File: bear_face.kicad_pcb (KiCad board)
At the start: 2 copper layers, 301.7 x 112.6 mm, 275 parts, among them J1 USB_B_Micro, Q1 2N7002, SW1 SW_Push, U1 ATmega32U4-AU, Y1 16MHz

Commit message: Short diode, resistor tracks added for ease of starting over
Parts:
- moved R8 0.79 mm to (219.8, 88.2)
- turned R64 to 180 degrees
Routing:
- net Net-(MX81-Pad4): track 0.00 -> 23.1 mm
- net Net-(MX78-Pad4): track 0.00 -> 21.8 mm
- net Net-(MX65-Pad4): track 0.00 -> 21.8 mm
- net Net-(MX64-Pad4): track 0.00 -> 21.8 mm
- net Net-(MX63-Pad4): track 0.00 -> 21.8 mm
- net Net-(MX75-Pad4): track 0.00 -> 21.8 mm
- net Net-(MX79-Pad4): track 0.00 -> 21.8 mm
- net Net-(MX80-Pad4): track 0.00 -> 21.8 mm
- net Net-(MX77-Pad4): track 0.00 -> 21.8 mm
- net Net-(MX76-Pad4): track 0.00 -> 21.8 mm
- net Net-(MX82-Pad4): track 0.00 -> 19.8 mm
- net Net-(MX83-Pad4): track 0.00 -> 14.9 mm
- net Net-(MX74-Pad4): track 0.00 -> 14.9 mm
- net Net-(D72-Pad2): track 0.00 -> 13.2 mm
- net Net-(D73-Pad2): track 0.00 -> 13.2 mm
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
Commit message: Short traces flipped
Flipped short trace from LED to resistor to B.Cu
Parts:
- moved Q1 10.3 mm to (96.0, 160.4)
- moved R88 5.55 mm to (96.0, 151.7), turned to 90 degrees
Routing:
- net ROW0: track 0.00 -> 303.8 mm
- net +5V: track 0.00 -> 303.2 mm
- net LEDOUT: track 0.00 -> 294.2 mm
- net Net-(MX81-Pad4): track 23.1 -> 0.00 mm
- net Net-(MX78-Pad4): track 21.8 -> 0.00 mm
- net Net-(MX65-Pad4): track 21.8 -> 0.00 mm
- net Net-(MX64-Pad4): track 21.8 -> 0.00 mm
- net Net-(MX63-Pad4): track 21.8 -> 0.00 mm
- net Net-(MX75-Pad4): track 21.8 -> 0.00 mm
- net Net-(MX79-Pad4): track 21.8 -> 0.00 mm
- net Net-(MX80-Pad4): track 21.8 -> 0.00 mm
- net Net-(MX77-Pad4): track 21.8 -> 0.00 mm
- net Net-(MX76-Pad4): track 21.8 -> 0.00 mm
- net Net-(MX82-Pad4): track 19.8 -> 0.00 mm
- net Net-(MX83-Pad4): track 14.9 -> 0.00 mm
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
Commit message: Rows mostly drawn
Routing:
- net +5V: track 303.2 -> 1523.1 mm
- net LEDOUT: track 294.2 -> 1432.1 mm
- net ROW2: track 0.00 -> 287.0 mm
- net ROW3: track 0.00 -> 284.7 mm
- net ROW1: track 0.00 -> 275.6 mm
- net ROW4: track 0.00 -> 231.4 mm
- net ROW5: track 0.00 -> 215.0 mm
- net ROW0: track 303.8 -> 286.3 mm
- net Net-(MX73-Pad4): track 0.00 -> 5.81 mm
- net Net-(MX71-Pad4): track 0.00 -> 5.81 mm
- net Net-(MX70-Pad4): track 0.00 -> 5.81 mm
- net Net-(MX68-Pad4): track 0.00 -> 5.81 mm
- net Net-(MX67-Pad4): track 0.00 -> 5.81 mm
- net Net-(MX72-Pad4): track 0.00 -> 5.81 mm
- net Net-(MX69-Pad4): track 0.00 -> 5.81 mm
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
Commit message: Columns drawn
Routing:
- net COL2: track 0.00 -> 114.0 mm
- net COL9: track 0.00 -> 111.0 mm
- net COL10: track 0.00 -> 111.0 mm
- net COL5: track 0.00 -> 110.1 mm
- net COL12: track 0.00 -> 107.1 mm
- net COL11: track 0.00 -> 107.1 mm
- net COL0: track 0.00 -> 106.1 mm
- net COL13: track 0.00 -> 105.1 mm
- net COL14: track 0.00 -> 97.2 mm
- net COL1: track 0.00 -> 93.9 mm
- net COL8: track 0.00 -> 90.0 mm
- net COL7: track 0.00 -> 90.0 mm
- net COL6: track 0.00 -> 90.0 mm
- net COL4: track 0.00 -> 90.0 mm
- net COL3: track 0.00 -> 90.0 mm
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
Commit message: DRC checked, tracks updated
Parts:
- moved C1 0.37 mm to (166.2, 173.9)
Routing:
- net ROW3: track 284.7 -> 286.0 mm
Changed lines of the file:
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@@
     (thickness 1.6)
     (drawings 14)
-    (tracks 1520)
+    (tracks 1523)
     (zones 0)
     (modules 275)
@@
   )
   (module Capacitor_SMD:C_0805_2012Metric (layer B.Cu)
-    (at 166.1795 165.95725 180)
+    (at 166.1795 165.9517 180)
     (descr "Capacitor SMD 0805 (2012 Metric), square (rectangular) end terminal, IPC_7351 nominal, (Body size source: https://docs.google.com/spreadsheets/d/1BsfQQcO9C6DZCsRaXUlFlo91Tg2WpOkGARC1WS5S8t0/edit?usp=sharing), generated with kicad-footprint-generator")
     (tags capacitor)
@@
   )
   (module Capacitor_SMD:C_0805_2012Metric (layer B.Cu)
-    (at 166.1795 173.51375)
+    (at 166.1795 173.8887)
     (descr "Capacitor SMD 0805 (2012 Metric), square (rectangular) end terminal, IPC_7351 nominal, (Body size source: https://docs.google.com/spreadsheets/d/1BsfQQcO9C6DZCsRaXUlFlo91Tg2WpOkGARC1WS5S8t0/edit?usp=sharing), generated with kicad-footprint-generator")
     (tags capacitor)
@@
   (segment (start 148.3995 138.811) (end 149.224999 137.985501) (width 0.254) (layer F.Cu) (net 88))
   (segment (start 165.862 138.811) (end 169.037 138.811) (width 0.254) (layer F.Cu) (net 88))
-  (segment (start 175.080838 138.811) (end 175.090339 138.801499) (width 0.254) (layer F.Cu) (net 88))
-  (segment (start 169.037 138.811) (end 175.080838 138.811) (width 0.254) (layer F.Cu) (net 88))
   (segment (start 223.774001 137.985501) (end 224.5995 138.811) (width 0.254) (layer F.Cu) (net 88))
   (segment (start 206.374999 137.985501) (end 223.774001 137.985501) (width 0.254) (layer F.Cu) (net 88))
   (segment (start 205.5495 138.811) (end 206.374999 137.985501) (width 0.254) (layer F.Cu) (net 88))
-  (segment (start 205.5495 138.811) (end 203.7715 138.811) (width 0.254) (layer F.Cu) (net 88))
-  (segment (start 175.090339 138.801499) (end 203.7715 138.811) (width 0.254) (layer F.Cu) (net 88))
   (segment (start 242.824001 137.985501) (end 243.6495 138.811) (width 0.254) (layer F.Cu) (net 88))
   (segment (start 225.424999 137.985501) (end 242.824001 137.985501) (width 0.254) (layer F.Cu) (net 88))
@@
   (segment (start 332.923183 138.811) (end 343.662 138.811) (width 0.254) (layer F.Cu) (net 88))
   (segment (start 331.75575 138.811) (end 332.923183 138.811) (width 0.254) (layer F.Cu) (net 88))
+  (segment (start 169.862499 137.985501) (end 182.626001 137.985501) (width 0.254) (layer F.Cu) (net 88))
+  (segment (start 182.626001 137.985501) (end 183.4515 138.811) (width 0.254) (layer F.Cu) (net 88))
+  (segment (start 169.037 138.811) (end 169.862499 137.985501) (width 0.254) (layer F.Cu) (net 88))
+  (segment (start 190.372999 137.985501) (end 189.5475 138.811) (width 0.254) (layer F.Cu) (net 88))
+  (segment (start 204.724001 137.985501) (end 190.372999 137.985501) (width 0.254) (layer F.Cu) (net 88))
+  (segment (start 205.5495 138.811) (end 204.724001 137.985501) (width 0.254) (layer F.Cu) (net 88))
+  (segment (start 183.4515 138.811) (end 189.5475 138.811) (width 0.254) (layer F.Cu) (net 88))
   (segment (start 138.049001 157.035501) (end 138.8745 157.861) (width 0.254) (layer F.Cu) (net 89))
   (segment (start 120.649999 157.035501) (end 138.049001 157.035501) (width 0.254) (layer F.Cu) (net 89))

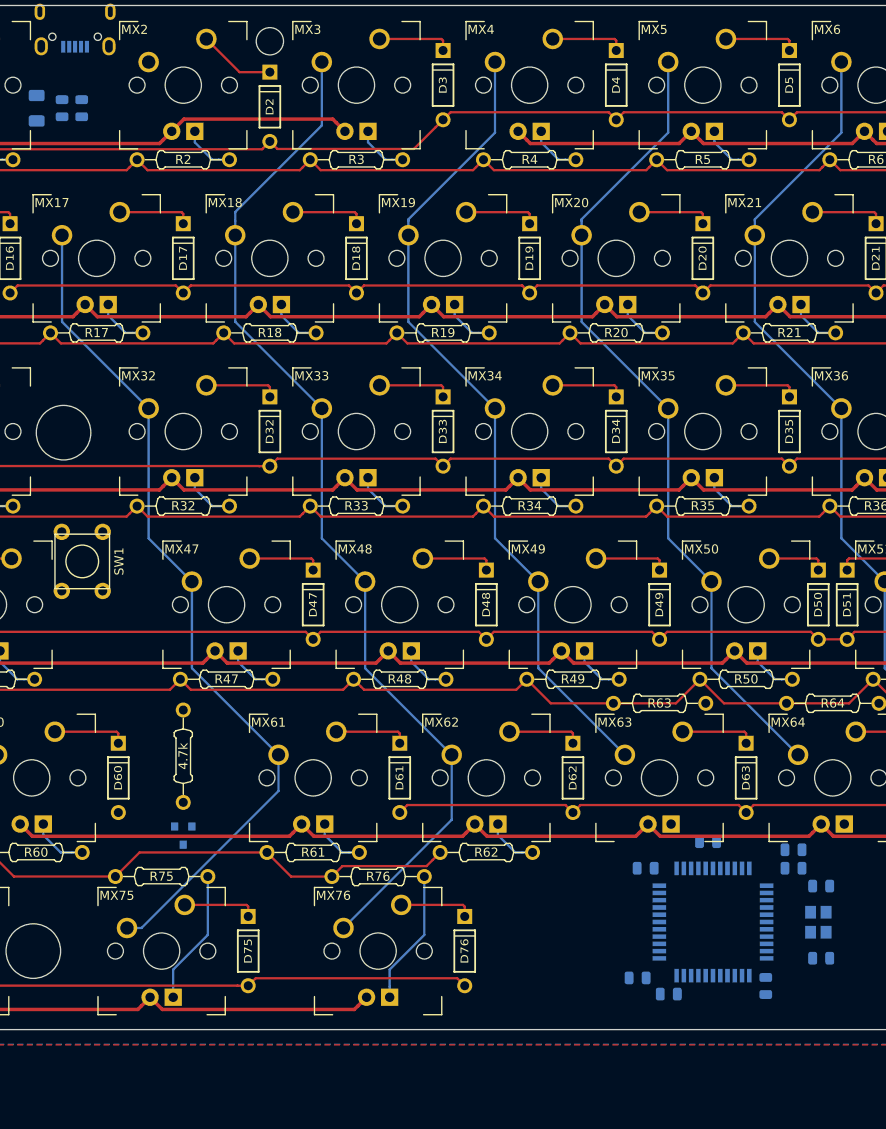
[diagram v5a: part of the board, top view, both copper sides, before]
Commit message: Changed MCU components back to SMD
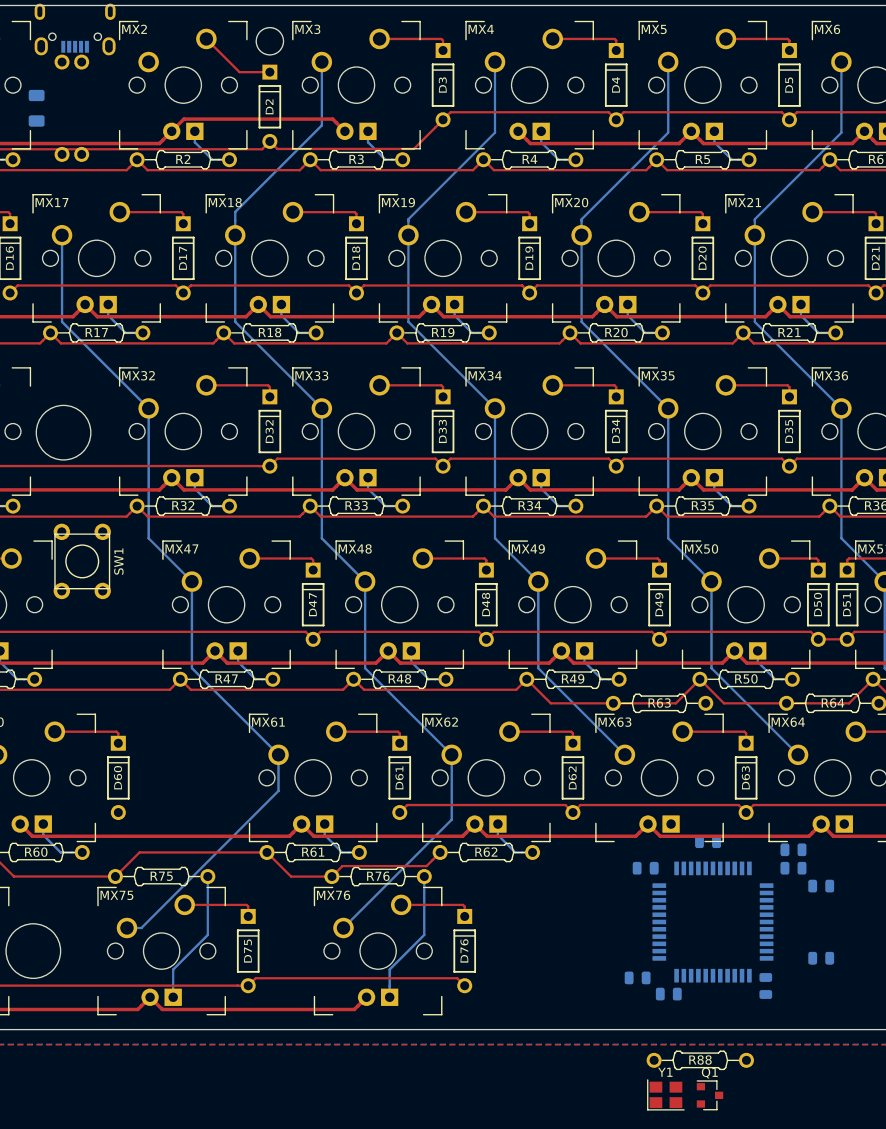
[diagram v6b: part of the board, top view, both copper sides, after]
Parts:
- Q1, Y1: moved to F.Cu
- R85, R86: footprint Resistor_SMD:R_0805_2012Metric -> bear_face_parts:Resistor-THT
- R88: footprint Keebio-Parts:Resistor -> bear_face_parts:Resistor-THT
- moved R88 66.0 mm to (152.9, 185.1), turned to 0 degrees
- moved Q1 64.6 mm to (154.0, 189.0), turned to 0 degrees
- moved Y1 25.3 mm to (149.1, 188.9), turned to 0 degrees
